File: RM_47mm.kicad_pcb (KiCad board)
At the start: 2 copper layers, 40 x 40 mm, 31 parts, among them J1 USB_C_Receptacle_USB2.0, J2 SWD, SW1 RESET, SW2 WKUP, U1 STM32F103C8Tx, U2 AMS1117-3.3

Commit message: Four
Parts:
- C10, C11, C12, C9, R1, R2, R3, R4, R5: moved to B.Cu
- moved R1 118.2 mm to (157.5, 105.8), turned to 180 degrees
- moved C10 114.5 mm to (157.5, 101.1), turned to -90 degrees
- moved C9 114.0 mm to (157.5, 97.6), turned to -90 degrees
- moved SW1 113.6 mm to (155.0, 110.0)
- moved C12 113.5 mm to (157.5, 104.1), turned to 180 degrees
- moved C11 104.9 mm to (152.5, 93.0), turned to 180 degrees
- moved R4 98.4 mm to (147.6, 93.0)
- moved R5 98.3 mm to (141.4, 104.1), turned to 180 degrees
- moved U2 98.2 mm to (160.0, 91.4), turned to -45 degrees
- moved R3 95.2 mm to (141.4, 94.0)
- moved R2 95.2 mm to (141.4, 91.4), turned to 180 degrees
- moved SW2 88.8 mm to (145.0, 110.0)
- moved J1 58.9 mm to (150.0, 83.0), turned to 0 degrees
- moved J2 49.6 mm to (133.5, 100.0), turned to 90 degrees
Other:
- board text added: "3V3"
- board text added: "GND"
- board text added: "SWCLK"
- board text added: "SWDIO"

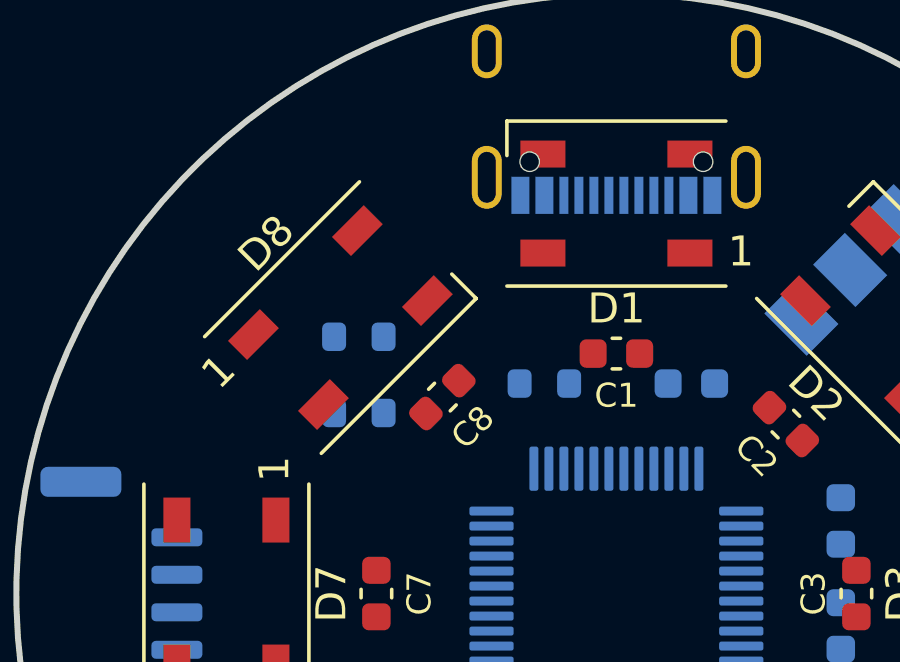
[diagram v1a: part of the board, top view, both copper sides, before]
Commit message: Add to 4 Plane & Cancle 网格限制
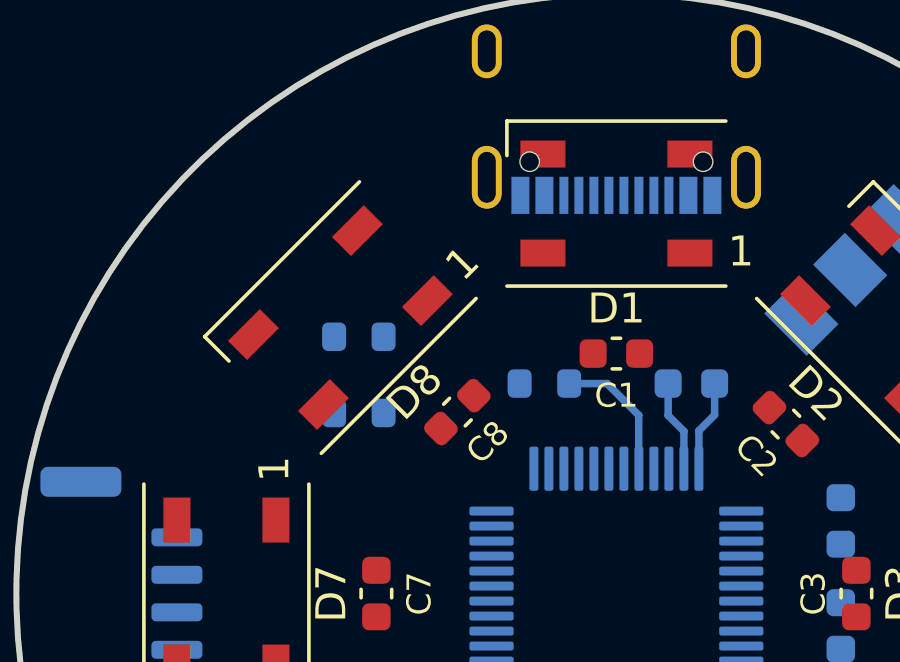
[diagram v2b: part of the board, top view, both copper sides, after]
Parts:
- moved C8 0.71 mm to (144.7, 94.0)
- turned D8 to -135 degrees
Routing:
- net /BOOT0: track 0.00 -> 4.54 mm
- net Earth: track 0.00 -> 3.05 mm
- net /VCC_3V3: track 0.00 -> 3.05 mm
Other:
- copper layers 2 -> 4
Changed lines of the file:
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@@
 (kicad_pcb (version 20221018) (generator pcbnew)
   (general
-    (thickness 1.6)
+    (thickness 0.19)
   )
   (paper "A4")
   (layers
     (0 "F.Cu" signal "F.Cu（顶层铜层）")
+    (1 "In1.Cu" power "In1.Cu(GND Plane)")
+    (2 "In2.Cu" power "In2.Cu(VCC Plane)")
     (31 "B.Cu" signal "B.Cu（底层铜层）")
     (32 "B.Adhes" user "B.Adhesive（粘合层）")
@@
     (48 "B.Fab" user "B.Fab（生产层）")
     (49 "F.Fab" user "F.Fab（生产层）")
-    (50 "User.1" user)
-    (51 "User.2" user)
-    (52 "User.3" user)
-    (53 "User.4" user)
-    (54 "User.5" user)
-    (55 "User.6" user)
-    (56 "User.7" user)
-    (57 "User.8" user)
-    (58 "User.9" user)
   )
   (setup
+    (stackup
+      (layer "F.SilkS" (type "Top Silk Screen"))
+      (layer "F.Paste" (type "Top Solder Paste"))
+      (layer "F.Mask" (type "Top Solder Mask") (thickness 0.01))
+      (layer "F.Cu" (type "copper") (thickness 0.035))
+      (layer "dielectric 1" (type "prepreg") (thickness 0.01) (material "FR4") (epsilon_r 4.5) (loss_tangent 0.02))
+      (layer "In1.Cu" (type "copper") (thickness 0.035))
+      (layer "dielectric 2" (type "core") (thickness 0.01) (material "FR4") (epsilon_r 4.5) (loss_tangent 0.02))
+      (layer "In2.Cu" (type "copper") (thickness 0.035))
+      (layer "dielectric 3" (type "prepreg") (thickness 0.01) (material "FR4") (epsilon_r 4.5) (loss_tangent 0.02))
+      (layer "B.Cu" (type "copper") (thickness 0.035))
+      (layer "B.Mask" (type "Bottom Solder Mask") (thickness 0.01))
+      (layer "B.Paste" (type "Bottom Solder Paste"))
+      (layer "B.SilkS" (type "Bottom Silk Screen"))
+      (copper_finish "None")
+      (dielectric_constraints no)
+    )
     (pad_to_mask_clearance 0)
     (pcbplotparams
@@
   )
   (footprint "LED_SMD:LED_WS2812B_PLCC4_5.0x5.0mm_P3.2mm" (layer "F.Cu")
-    (at 140.8 90.8 45)
+    (at 140.8 90.8 -135)
     (descr "5.0mm x 5.0mm Addressable RGB LED NeoPixel, https://cdn-shop.adafruit.com/datasheets/WS2812B.pdf")
     (tags "LED RGB NeoPixel PLCC-4 5050")
@@
     (fp_circle (center 0 0) (end 0 -2)
       (stroke (width 0.1) (type solid)) (fill none) (layer "F.Fab"))
-    (pad "1" smd rect (at -2.45 -1.65 45) (size 1.5 0.9) (layers "F.Cu" "F.Paste" "F.Mask")
+    (pad "1" smd rect (at -2.45 -1.65 225) (size 1.5 0.9) (layers "F.Cu" "F.Paste" "F.Mask")
       (net 2 "/VCC_3V3") (pinfunction "VDD") (pintype "power_in"))
-    (pad "2" smd rect (at -2.45 1.65 45) (size 1.5 0.9) (layers "F.Cu" "F.Paste" "F.Mask")
+    (pad "2" smd rect (at -2.45 1.65 225) (size 1.5 0.9) (layers "F.Cu" "F.Paste" "F.Mask")
       (net 10 "unconnected-(D8-DOUT-Pad2)") (pinfunction "DOUT") (pintype "output+no_connect"))
-    (pad "3" smd rect (at 2.45 1.65 45) (size 1.5 0.9) (layers "F.Cu" "F.Paste" "F.Mask")
+    (pad "3" smd rect (at 2.45 1.65 225) (size 1.5 0.9) (layers "F.Cu" "F.Paste" "F.Mask")
       (net 3 "Earth") (pinfunction "VSS") (pintype "power_in"))
-    (pad "4" smd rect (at 2.45 -1.65 45) (size 1.5 0.9) (layers "F.Cu" "F.Paste" "F.Mask")
+    (pad "4" smd rect (at 2.45 -1.65 225) (size 1.5 0.9) (layers "F.Cu" "F.Paste" "F.Mask")
       (net 60 "Net-(D7-DOUT)") (pinfunction "DIN") (pintype "input"))
     (model "${KICAD7_3DMODEL_DIR}/LED_SMD.3dshapes/LED_WS2812B_PLCC4_5.0x5.0mm_P3.2mm.wrl"
@@
   )
   (footprint "Capacitor_SMD:C_0603_1608Metric" (layer "F.Cu")
-    (at 144.2 93.45 45)
+    (at 144.7 93.95 45)
     (descr "Capacitor SMD 0603 (1608 Metric), square (rectangular) end terminal, IPC_7351 nominal, (Body size source: IPC-SM-782 page 76, https://www.pcb-3d.com/wordpress/wp-content/uploads/ipc-sm-782a_amendment_1_and_2.pdf), generated with kicad-footprint-generator")
     (tags "capacitor")
@@
     )
   )
+  (segment (start 153.275 94.043946) (end 152.75 94.568946) (width 0.25) (layer "B.Cu") (net 2))
+  (segment (start 152.75 94.568946) (end 152.75 95.8375) (width 0.25) (layer "B.Cu") (net 2))
+  (segment (start 153.275 93) (end 153.275 94.043946) (width 0.25) (layer "B.Cu") (net 2))
+  (segment (start 152.25 94.588612) (end 152.25 95.8375) (width 0.25) (layer "B.Cu") (net 3))
+  (segment (start 151.725 94.063612) (end 152.25 94.588612) (width 0.25) (layer "B.Cu") (net 3))
+  (segment (start 151.725 93) (end 151.725 94.063612) (width 0.25) (layer "B.Cu") (net 3))
+  (segment (start 148.425 93) (end 149.689154 93) (width 0.25) (layer "B.Cu") (net 13))
+  (segment (start 150.744812 94.055658) (end 150.744812 95.832312) (width 0.25) (layer "B.Cu") (net 13))
+  (segment (start 150.744812 95.832312) (end 150.75 95.8375) (width 0.25) (layer "B.Cu") (net 13))
+  (segment (start 149.689154 93) (end 150.744812 94.055658) (width 0.25) (layer "B.Cu") (net 13))
 )

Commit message: 连线STEP-1
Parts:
- added C13: 100nf, Capacitor_SMD:C_0603_1608Metric, B.Cu at (150.0, 107.3)
- added R6: 4.7kΩ, Resistor_SMD:R_0603_1608Metric, B.Cu at (136.3, 109.7)
- added R7: 1kΩ, Resistor_SMD:R_0603_1608Metric, B.Cu at (151.0, 110.0)
- added SW3: SW_Push_Dual, Button_Switch_THT:SW_Tactile_SPST_Angled_PTS645Vx39-2LFS, B.Cu at (147.7, 118.4)
- C12: value 0.1uf -> 100nf
- R1: value 10k -> 10kΩ
- moved R5 9.58 mm to (149.0, 110.0), turned to -90 degrees
- moved R3 7.84 mm to (142.0, 101.8), turned to -90 degrees
- moved R2 7.08 mm to (142.0, 98.5), turned to 90 degrees
- moved D5 1.20 mm to (150.0, 111.8)
- moved SW1 1.00 mm to (156.0, 110.0)
- moved SW2 1.00 mm to (144.0, 110.0)
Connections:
- J1 pad S1: unconnected-(J1-SHIELD-PadS1) -> Earth
- U1 pad 32: unconnected-(U1-PA11-Pad32) -> /Button_LED
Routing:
- net Earth: track 3.05 -> 27.4 mm, vias 0 -> 14
- net /VCC_3V3: track 3.05 -> 18.0 mm, vias 0 -> 6
- net /SWCLK: track 0.00 -> 13.5 mm
- net /SWDIO: track 0.00 -> 7.33 mm
- net /RESET: track 0.00 -> 5.83 mm
- net /WKUP: track 0.00 -> 4.15 mm
- net Net-(SW3-3): track 0.00 -> 1.95 mm

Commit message: Finish All
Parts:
- added G***: LOGO, Library:R-Logo_8mm, F.Cu at (150.3, 99.9)
- added G***: LOGO, Library:QianLi_20mm, B.Cu at (164.6, 101.0)
- moved C12 12.9 mm to (144.9, 107.2)
- moved R1 12.6 mm to (144.9, 105.5)
- moved SW1 12.0 mm to (144.0, 110.0)
- moved SW2 12.0 mm to (156.0, 110.0)
- moved C13 12.0 mm to (138.0, 106.5), turned to 90 degrees
- moved R7 11.7 mm to (139.8, 106.5), turned to 90 degrees
- moved R2 3.31 mm to (142.0, 101.8), turned to -90 degrees
- moved R3 3.24 mm to (142.0, 98.6), turned to 90 degrees
- moved R6 2.75 mm to (139.0, 108.9), turned to 0 degrees
- moved D1 1.00 mm to (150.0, 86.0)
- moved R5 0.34 mm to (149.3, 110.2)
- moved C10 0.06 mm to (157.5, 101.0), turned to 90 degrees
- turned C6 to -45 degrees
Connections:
- J2 pad 2: /SWCLK -> /SWDIO
- J2 pad 3: /SWDIO -> /SWCLK
- J2 pad MP: (no net) -> Earth
- R2 pad 2: /SWCLK -> /SWDIO
- R3 pad 1: /SWDIO -> /SWCLK
- SW3 pad : (no net) -> Earth
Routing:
- net /VCC_3V3: track 18.0 -> 95.5 mm, vias 6 -> 11
- net Earth: track 27.4 -> 102.2 mm, vias 14 -> 10
- net Net-(C1-Pad1): track 0.00 -> 48.4 mm
- net Net-(SW3-3): track 1.95 -> 22.2 mm
- net /VCC_5V: track 0.00 -> 18.2 mm
- net /RESET: track 5.83 -> 21.7 mm
- net /LED_IN: track 0.00 -> 11.0 mm, vias 0 -> 1
- net /Button_LED: track 0.00 -> 10.1 mm
- net /WKUP: track 4.15 -> 13.4 mm
- net Net-(D1-DOUT): track 0.00 -> 8.79 mm
- net Net-(D4-DOUT): track 0.00 -> 7.43 mm
- net /SWDIO: track 7.33 -> 14.0 mm
- net Net-(D6-DOUT): track 0.00 -> 6.49 mm
- net Net-(D2-DOUT): track 0.00 -> 6.49 mm
- net Net-(D7-DOUT): track 0.00 -> 6.48 mm
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- added copper zone on In2.Cu, net /VCC_3V3
- added copper zone on In1.Cu, net Earth
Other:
- board text added: "Mr.Dynamic©"
- board text added: "重大·千里"
